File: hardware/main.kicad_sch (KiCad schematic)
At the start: 430 parts, among them J1 DS1128-09-S8B8X, J10 AS0BC21-S30BM-7H, J2 DS1128-09-S8B8X, J3 DS1128-09-S8B8X, J4 98424-G52-04ALF, J5 miniPCI-E_52P_5.2, J8 USB_C_Receptacle, J9 TYPE-C-31-M-12, Q1 SSM6J501NU, Q3 FDV301N, SW1 TS-1187A-B-A-B, SW2 TS-1187A-B-A-B, U1 SSD1306-OLED-0.91, U10 W25Q256FVEIG, U12 TPD2EUSB30, U13 TPD2EUSB30, U14 TPD2EUSB30, U15 IP5328P, U2 MT7621A, U3 TPS63020, U4 TPS63020, U5 MT3420B, U6 MT3420B, U7 MT3420B, U8 MT3420B, U9 NT5CB64M16FP-DH (!), Y1 X322540MPB4SI

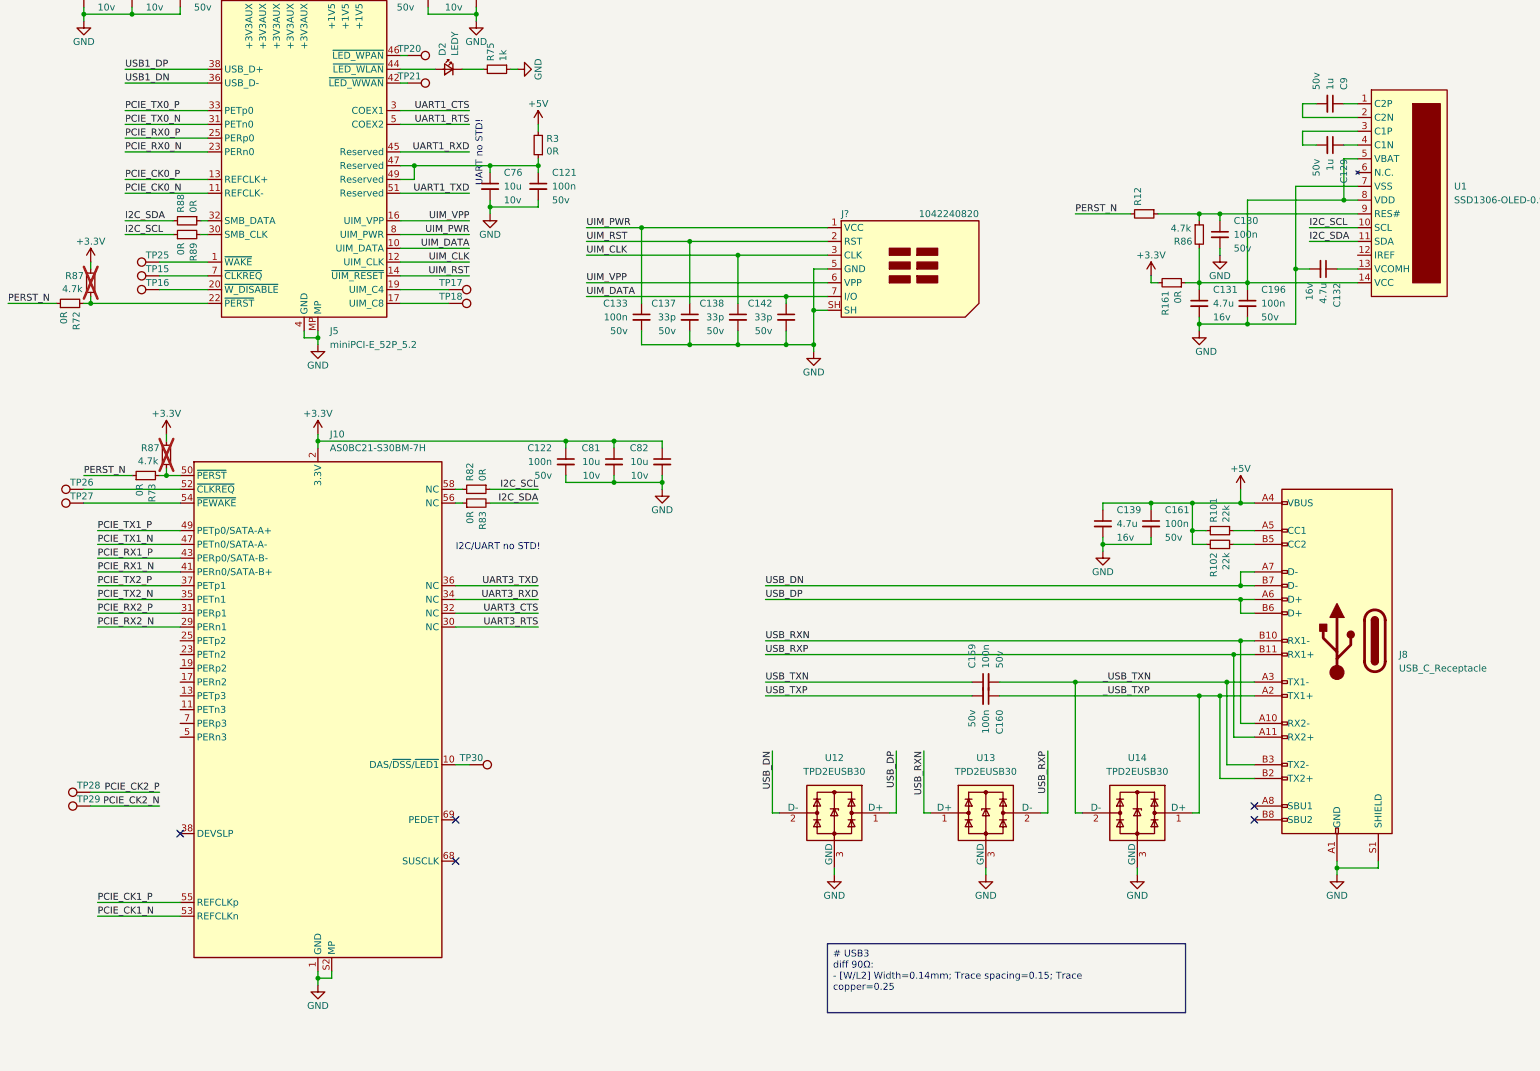
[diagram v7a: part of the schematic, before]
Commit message: update pin layout
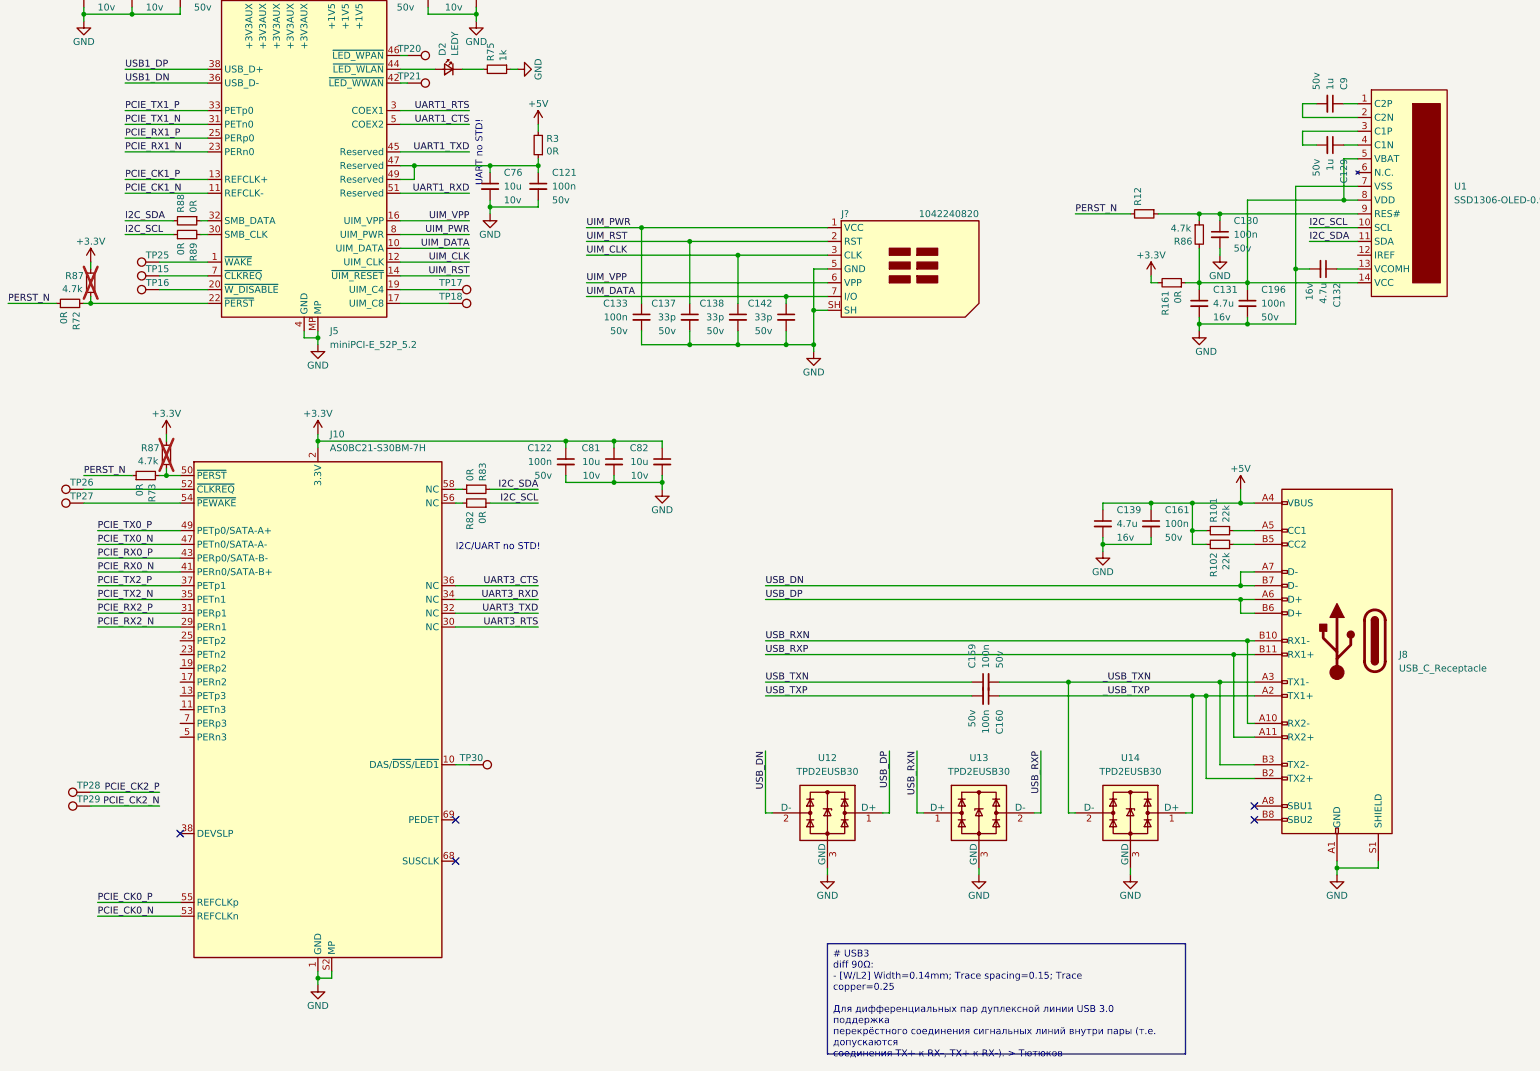
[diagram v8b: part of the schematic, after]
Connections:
- net PCIE_CK0_N: now also J10.53 (REFCLKn); no longer J5.11 (REFCLK-)
- net PCIE_CK0_P: now also J10.55 (REFCLKp); no longer J5.13 (REFCLK+)
- net PCIE_CK1_N: now also J5.11 (REFCLK-); no longer J10.53 (REFCLKn)
- net PCIE_CK1_P: now also J5.13 (REFCLK+); no longer J10.55 (REFCLKp)
- net PCIE_RX0_N: now also J10.41 (PERn0/SATA-B+); no longer J5.23 (PERn0)
- net PCIE_RX0_P: now also J10.43 (PERp0/SATA-B-); no longer J5.25 (PERp0)
- net PCIE_RX1_N: now also J5.23 (PERn0); no longer J10.41 (PERn0/SATA-B+)
- net PCIE_RX1_P: now also J5.25 (PERp0); no longer J10.43 (PERp0/SATA-B-)
- net PCIE_TX0_N: now also J10.47 (PETn0/SATA-A-); no longer J5.31 (PETn0)
- net PCIE_TX0_P: now also J10.49 (PETp0/SATA-A+); no longer J5.33 (PETp0)
- net PCIE_TX1_N: now also J5.31 (PETn0); no longer J10.47 (PETn0/SATA-A-)
- net PCIE_TX1_P: now also J5.33 (PETp0); no longer J10.49 (PETp0/SATA-A+)
- net UART1_CTS: now also J5.5 (COEX2); no longer J5.3 (COEX1)
- net UART1_RTS: now also J5.3 (COEX1); no longer J5.5 (COEX2)
- net UART1_RXD: now also J5.51 (Reserved); no longer J5.45 (Reserved)
- net UART1_TXD: now also J5.45 (Reserved); no longer J5.51 (Reserved)
- net UART3_CTS: now also J10.36 (NC); no longer J10.32 (NC)
- net UART3_TXD: now also J10.32 (NC); no longer J10.36 (NC)
- net at R82.2: now also J10.56 (NC); no longer J10.58 (NC)
- net at R83.1: now also J10.58 (NC); no longer J10.56 (NC)
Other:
- moved on the sheet: R82, R83, U12, U13, U14
